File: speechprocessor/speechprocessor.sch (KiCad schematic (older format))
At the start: 4 parts

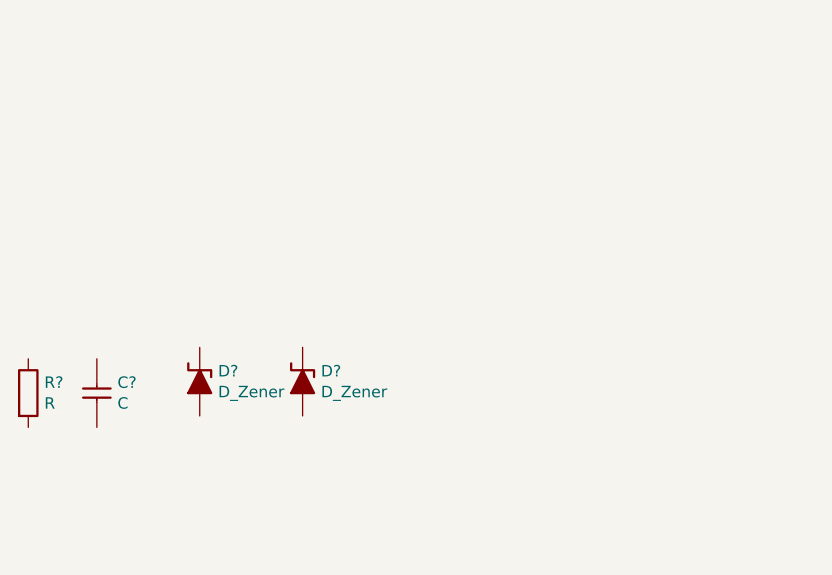
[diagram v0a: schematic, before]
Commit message: First iteration of speechprocessor
Signed-off-by: Andres Gongora <mail@andresgongora.com>
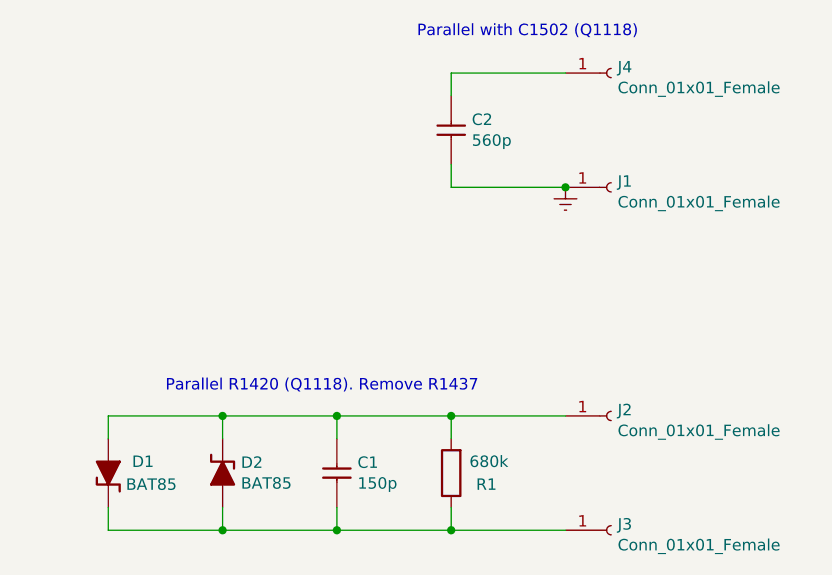
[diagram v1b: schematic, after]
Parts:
- added C2: 560p, NicerFootprints:SMD_0805, symbol NicerLibrary:C
- added J1, J2, J3, J4: Conn_01x01_Female, symbol Connector:Conn_01x01_Female
- C1: renamed from C?; value C -> 150p; footprint (none) -> NicerFootprints:SMD_0805
- D1, D2: renamed from D?; value D_Zener -> BAT85; footprint (none) -> NicerFootprints:SMD_0805_Polarized
- R1: renamed from R?; value R -> 680k; footprint (none) -> NicerFootprints:SMD_0805
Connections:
- net at C1.1: now also D1.2 (A), D2.1 (K), R1.2, J2.1 (Pin_1)
- net at C1.2: now also D1.1 (K), D2.2 (A), R1.1, J3.1 (Pin_1)
- new net: C2.1, J4.1 (Pin_1)
- new net Earth: C2.2, J1.1 (Pin_1)
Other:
- note added: "Parallel R1420 (Q1118). Remove R1437"
- note added: "Parallel with C1502 (Q1118)"
- moved on the sheet: C1, D1, D2, R1
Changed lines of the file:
@@
 $EndDescr
 $Comp
-L NicerLibrary:C C?
+L NicerLibrary:C C1
 U 1 1 5FC2A013
-P 4450 2900
-F 0 "C?" H 4540 2946 50  0000 L CNN
-F 1 "C" H 4540 2855 50  0000 L CNN
-F 2 "" H 4488 2750 50  0001 C CNN
-F 3 "~" H 4450 2900 50  0001 C CNN
-	1    4450 2900
+P 5500 3250
+F 0 "C1" H 5590 3296 50  0000 L CNN
+F 1 "150p" H 5590 3205 50  0000 L CNN
+F 2 "NicerFootprints:SMD_0805" H 5538 3100 50  0001 C CNN
+F 3 "~" H 5500 3250 50  0001 C CNN
+	1    5500 3250
 	1    0    0    -1
 $EndComp
 $Comp
-L NicerLibrary:D_Zener D?
+L NicerLibrary:D_Zener D1
 U 1 1 5FC2A634
-P 4900 2850
-F 0 "D?" H 4980 2896 50  0000 L CNN
-F 1 "D_Zener" H 4980 2805 50  0000 L CNN
-F 2 "" V 4900 2850 50  0001 C CNN
-F 3 "~" V 4900 2850 50  0001 C CNN
-	1    4900 2850
+P 4500 3250
+F 0 "D1" H 4300 3200 50  0000 L CNN
+F 1 "BAT85" H 4200 3300 50  0000 L CNN
+F 2 "NicerFootprints:SMD_0805_Polarized" V 4500 3250 50  0001 C CNN
+F 3 "~" V 4500 3250 50  0001 C CNN
+	1    4500 3250
+	-1   0    0    1
+$EndComp
+$Comp
+L NicerLibrary:D_Zener D2
+U 1 1 5FC2A90D
+P 5000 3250
+F 0 "D2" H 5080 3296 50  0000 L CNN
+F 1 "BAT85" H 5080 3205 50  0000 L CNN
+F 2 "NicerFootprints:SMD_0805_Polarized" V 5000 3250 50  0001 C CNN
+F 3 "~" V 5000 3250 50  0001 C CNN
+	1    5000 3250
 	1    0    0    -1
 $EndComp
 $Comp
-L NicerLibrary:D_Zener D?
-U 1 1 5FC2A90D
-P 5350 2850
-F 0 "D?" H 5430 2896 50  0000 L CNN
-F 1 "D_Zener" H 5430 2805 50  0000 L CNN
-F 2 "" V 5350 2850 50  0001 C CNN
-F 3 "~" V 5350 2850 50  0001 C CNN
-	1    5350 2850
+L NicerLibrary:R R1
+U 1 1 5FC2AF5F
+P 6000 3250
+F 0 "R1" H 5800 3300 50  0000 L CNN
+F 1 "680k" H 5750 3200 50  0000 L CNN
+F 2 "NicerFootprints:SMD_0805" V 5930 3250 50  0001 C CNN
+F 3 "~" H 6000 3250 50  0001 C CNN
+	1    6000 3250
+	-1   0    0    1
+$EndComp
+Wire Wire Line
+	4500 3100 4500 3000
+Wire Wire Line
+	4500 3000 5000 3000
+Wire Wire Line
+	6000 3100 6000 3000
+Connection ~ 6000 3000
+Wire Wire Line
+	5500 3100 5500 3000
+Connection ~ 5500 3000
+Wire Wire Line
+	5500 3000 6000 3000
+Wire Wire Line
+	5000 3100 5000 3000
+Connection ~ 5000 3000
+Wire Wire Line
+	5000 3000 5500 3000
+Wire Wire Line
+	4500 3400 4500 3500
+Wire Wire Line
+	4500 3500 5000 3500
+Wire Wire Line
+	6000 3500 6000 3400
+Wire Wire Line
+	5500 3400 5500 3500
+Connection ~ 5500 3500
+Wire Wire Line
+	5500 3500 6000 3500
+Wire Wire Line
+	5000 3400 5000 3500
+Connection ~ 5000 3500
+Wire Wire Line
+	5000 3500 5500 3500
+$Comp
+L Connector:Conn_01x01_Female J1
+U 1 1 5FC39A90
+P 6700 2000
+F 0 "J1" H 6728 2026 50  0000 L CNN
+F 1 "Conn_01x01_Female" H 6728 1935 50  0000 L CNN
+F 2 "" H 6700 2000 50  0001 C CNN
+F 3 "~" H 6700 2000 50  0001 C CNN
+	1    6700 2000
 	1    0    0    -1
 $EndComp
 $Comp
-L NicerLibrary:R R?
-U 1 1 5FC2AF5F
-P 4150 2900
-F 0 "R?" H 4220 2946 50  0000 L CNN
-F 1 "R" H 4220 2855 50  0000 L CNN
-F 2 "" V 4080 2900 50  0001 C CNN
-F 3 "~" H 4150 2900 50  0001 C CNN
-	1    4150 2900
+L Connector:Conn_01x01_Female J2
+U 1 1 5FC3A28F
+P 6700 3000
+F 0 "J2" H 6728 3026 50  0000 L CNN
+F 1 "Conn_01x01_Female" H 6728 2935 50  0000 L CNN
+F 2 "" H 6700 3000 50  0001 C CNN
+F 3 "~" H 6700 3000 50  0001 C CNN
+	1    6700 3000
 	1    0    0    -1
 $EndComp
+$Comp
+L Connector:Conn_01x01_Female J3
+U 1 1 5FC3A848
+P 6700 3500
+F 0 "J3" H 6728 3526 50  0000 L CNN
+F 1 "Conn_01x01_Female" H 6728 3435 50  0000 L CNN
+F 2 "" H 6700 3500 50  0001 C CNN
+F 3 "~" H 6700 3500 50  0001 C CNN
+	1    6700 3500
+	1    0    0    -1
+$EndComp
+Wire Wire Line
+	6000 3000 6500 3000
+Wire Wire Line
+	6000 3500 6500 3500
+Connection ~ 6000 3500
+Wire Wire Line
+	6000 2000 6500 2000
+$Comp
+L power:Earth #PWR01
+U 1 1 5FC4054A
+P 6500 2000
+F 0 "#PWR01" H 6500 1750 50  0001 C CNN
+F 1 "Earth" H 6500 1850 50  0001 C CNN
+F 2 "" H 6500 2000 50  0001 C CNN
+F 3 "~" H 6500 2000 50  0001 C CNN
+	1    6500 2000
+	1    0    0    -1
+$EndComp
+Connection ~ 6500 2000
+$Comp
+L NicerLibrary:C C2
+U 1 1 5FC2AB32
+P 6000 1750
+F 0 "C2" H 6090 1796 50  0000 L CNN
+F 1 "560p" H 6090 1705 50  0000 L CNN
+F 2 "NicerFootprints:SMD_0805" H 6038 1600 50  0001 C CNN
+F 3 "~" H 6000 1750 50  0001 C CNN
+	1    6000 1750
+	1    0    0    -1
+$EndComp
+Wire Wire Line
+	6000 1900 6000 2000
+$Comp
+L Connector:Conn_01x01_Female J4
+U 1 1 5FC2B82B
+P 6700 1500
+F 0 "J4" H 6728 1526 50  0000 L CNN
+F 1 "Conn_01x01_Female" H 6728 1435 50  0000 L CNN
+F 2 "" H 6700 1500 50  0001 C CNN
+F 3 "~" H 6700 1500 50  0001 C CNN
+	1    6700 1500
+	1    0    0    -1
+$EndComp
+Wire Wire Line
+	6500 1500 6000 1500
+Wire Wire Line
+	6000 1500 6000 1600
+Text Notes 5850 1350 0    50   ~ 0
+Parallel with C1502 (Q1118)
+Text Notes 4750 2900 0    50   ~ 0
+Parallel R1420 (Q1118). Remove R1437
 $EndSCHEMATC
